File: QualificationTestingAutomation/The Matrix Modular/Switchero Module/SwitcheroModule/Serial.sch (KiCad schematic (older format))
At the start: 13 parts, among them IC1 MAX3109ETJ+, Q2 2N7002DW

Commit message: Cleaned up the libraries Cleaned up the tracks Adjusted footprints to the manufacturers minimum size.
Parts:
- C1: symbol TheMatrix-rescue:CAP-passive-SchematicAutomation-rescue -> SwitcheroModule-rescue:CAP-passive-SchematicAutomation-rescue-TheMatrix-rescue
- Q2: symbol TheMatrix-rescue:2N7002DW-dk_Transistors-FETs-MOSFETs-Arrays-SchematicAutomation-rescue -> SwitcheroModule-rescue:2N7002DW-dk_Transistors-FETs-MOSFETs-Arrays-SchematicAutomation-rescue-TheMatrix-rescue
- R10, R11, R12, R7, R8, R9: symbol TheMatrix-rescue:RESISTOR-passive-SchematicAutomation-rescue -> SwitcheroModule-rescue:RESISTOR-passive-SchematicAutomation-rescue-TheMatrix-rescue
- S1, S2, S3, S4: symbol TheMatrix-rescue:ATE1D-2M3-10-Z-dk_Toggle-Switches-SchematicAutomation-rescue -> SwitcheroModule-rescue:ATE1D-2M3-10-Z-dk_Toggle-Switches-SchematicAutomation-rescue-TheMatrix-rescue
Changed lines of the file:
@@
 ADD LEDS!!!!
 $Comp
-L TheMatrix-rescue:ATE1D-2M3-10-Z-dk_Toggle-Switches-SchematicAutomation-rescue S?
+L SwitcheroModule-rescue:ATE1D-2M3-10-Z-dk_Toggle-Switches-SchematicAutomation-rescue-TheMatrix-rescue S?
 U 1 1 5CB40D46
 P 3700 2600
@@
 	3200 2850 3450 2850
 $Comp
-L TheMatrix-rescue:ATE1D-2M3-10-Z-dk_Toggle-Switches-SchematicAutomation-rescue S?
+L SwitcheroModule-rescue:ATE1D-2M3-10-Z-dk_Toggle-Switches-SchematicAutomation-rescue-TheMatrix-rescue S?
 U 1 1 5CB40D93
 P 3650 3200
@@
 $EndComp
 $Comp
-L TheMatrix-rescue:ATE1D-2M3-10-Z-dk_Toggle-Switches-SchematicAutomation-rescue S?
+L SwitcheroModule-rescue:ATE1D-2M3-10-Z-dk_Toggle-Switches-SchematicAutomation-rescue-TheMatrix-rescue S?
 U 1 1 5CB40DA3
 P 4350 3700
@@
 $EndComp
 $Comp
-L TheMatrix-rescue:ATE1D-2M3-10-Z-dk_Toggle-Switches-SchematicAutomation-rescue S?
+L SwitcheroModule-rescue:ATE1D-2M3-10-Z-dk_Toggle-Switches-SchematicAutomation-rescue-TheMatrix-rescue S?
 U 1 1 5CB40DBC
 P 4300 2700
@@
 	4650 2600 4500 2600
 $Comp
-L TheMatrix-rescue:2N7002DW-dk_Transistors-FETs-MOSFETs-Arrays-SchematicAutomation-rescue Q?
+L SwitcheroModule-rescue:2N7002DW-dk_Transistors-FETs-MOSFETs-Arrays-SchematicAutomation-rescue-TheMatrix-rescue Q?
 U 1 1 5CA046D4
 P 2500 4500
@@
 AR Path="/5C90F514/5C94ECF2/5CA046D4" Ref="Q?"  Part="1"
 AR Path="/5C90F514/5CA046D4" Ref="Q2"  Part="1"
+AR Path="/5CA046D4" Ref="Q2"  Part="1"
 F 0 "Q2" H 2500 4987 60  0000 C CNN
 F 1 "2N7002DW" H 2500 4881 60  0000 C CNN
@@
 RS232INV
 $Comp
-L TheMatrix-rescue:RESISTOR-passive-SchematicAutomation-rescue R?
+L SwitcheroModule-rescue:RESISTOR-passive-SchematicAutomation-rescue-TheMatrix-rescue R?
 U 1 1 5CA046DE
 P 3100 4600
@@
 	3000 4600 2950 4600
 $Comp
-L TheMatrix-rescue:RESISTOR-passive-SchematicAutomation-rescue R?
+L SwitcheroModule-rescue:RESISTOR-passive-SchematicAutomation-rescue-TheMatrix-rescue R?
 U 1 1 5CA046E9
 P 2950 4700
@@
 $EndComp
 $Comp
-L TheMatrix-rescue:RESISTOR-passive-SchematicAutomation-rescue R?
+L SwitcheroModule-rescue:RESISTOR-passive-SchematicAutomation-rescue-TheMatrix-rescue R?
 U 1 1 5CA046FA
 P 2000 4900
@@
 	6800 2550 6800 2650
 $Comp
-L TheMatrix-rescue:CAP-passive-SchematicAutomation-rescue C?
+L SwitcheroModule-rescue:CAP-passive-SchematicAutomation-rescue-TheMatrix-rescue C?
 U 1 1 5CB0095F
 P 6400 2550
@@
 $EndComp
 $Comp
-L TheMatrix-rescue:RESISTOR-passive-SchematicAutomation-rescue R?
+L SwitcheroModule-rescue:RESISTOR-passive-SchematicAutomation-rescue-TheMatrix-rescue R?
 U 1 1 5CB06957
 P 6300 5150
@@
 SSINV
 $Comp
-L TheMatrix-rescue:RESISTOR-passive-SchematicAutomation-rescue R?
+L SwitcheroModule-rescue:RESISTOR-passive-SchematicAutomation-rescue-TheMatrix-rescue R?
 U 1 1 5CB11DAA
 P 3150 4300
@@
 SSINV
 $Comp
-L TheMatrix-rescue:RESISTOR-passive-SchematicAutomation-rescue R?
+L SwitcheroModule-rescue:RESISTOR-passive-SchematicAutomation-rescue-TheMatrix-rescue R?
 U 1 1 5CB232AB
 P 5650 3650

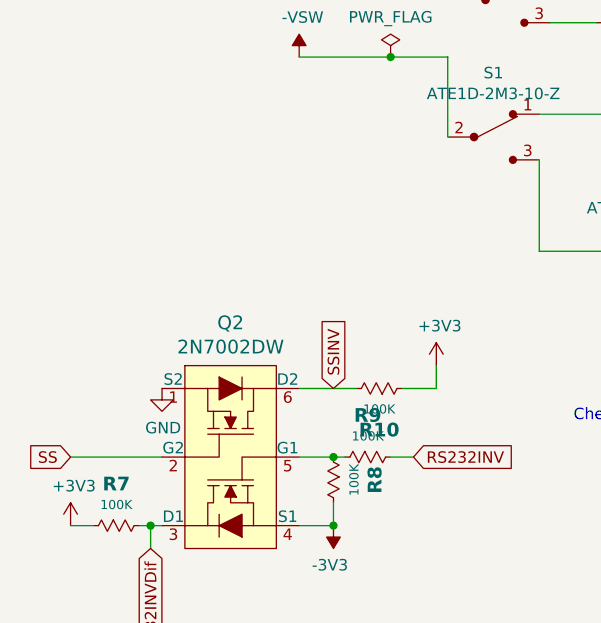
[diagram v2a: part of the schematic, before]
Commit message: Schematic Clean ups the layout needs to be changed
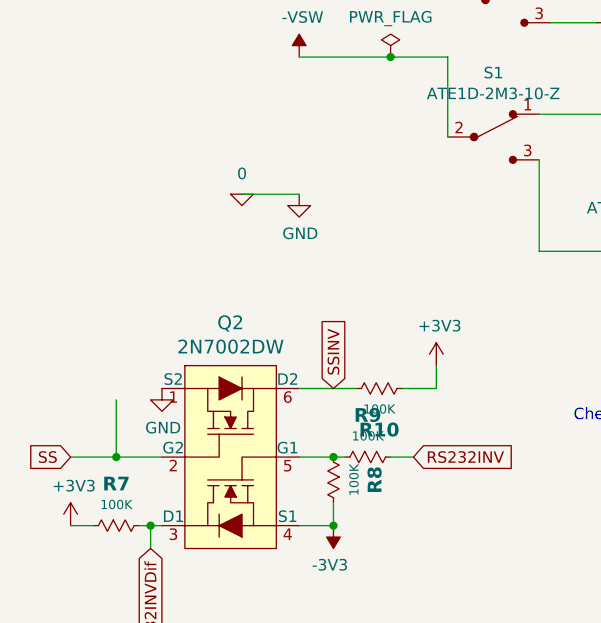
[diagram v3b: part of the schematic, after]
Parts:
- Q2: Spice_Lib_File (none) -> 2n7002dw.lib; Spice_Model (none) -> 2N7002DW; Spice_Netlist_Enabled (none) -> Y; Spice_Primitive (none) -> M
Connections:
- net GND renamed 0
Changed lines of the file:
@@
 F 11 "ON Semiconductor" H 2700 5600 60  0001 L CNN "Manufacturer"
 F 12 "Active" H 2700 5700 60  0001 L CNN "Status"
+F 13 "M" H 2500 4500 50  0001 C CNN "Spice_Primitive"
+F 14 "2N7002DW" H 2500 4500 50  0001 C CNN "Spice_Model"
+F 15 "Y" H 2500 4500 50  0001 C CNN "Spice_Netlist_Enabled"
+F 16 "2n7002dw.lib" H 2500 4500 50  0001 C CNN "Spice_Lib_File"
 	1    2500 4500
 	1    0    0    -1
@@
 SS
 Wire Wire Line
-	1800 4600 2200 4600
+	1800 4600 2000 4600
 Text GLabel 2950 4300 1    50   Input ~ 0
 SSINV
@@
 F 2 "" H 3400 4200 50  0001 C CNN
 F 3 "" H 3400 4200 50  0001 C CNN
+F 4 "V" H 3400 4200 50  0001 C CNN "Spice_Primitive"
+F 5 "dc 3.3" H 3400 4200 50  0001 C CNN "Spice_Model"
+F 6 "Y" H 3400 4200 50  0001 C CNN "Spice_Netlist_Enabled"
 	1    3400 4200
 	1    0    0    -1
@@
 	1    0    0    -1
 $EndComp
+$Comp
+L pspice:0 #GND0101
+U 1 1 5CB0FA23
+P 2550 3450
+F 0 "#GND0101" H 2550 3350 50  0001 C CNN
+F 1 "0" H 2550 3539 50  0000 C CNN
+F 2 "" H 2550 3450 50  0001 C CNN
+F 3 "~" H 2550 3450 50  0001 C CNN
+	1    2550 3450
+	1    0    0    -1
+$EndComp
+$Comp
+L power:GND #PWR?
+U 1 1 5CB10324
+P 2800 3450
+AR Path="/5C8DF48C/5CB10324" Ref="#PWR?"  Part="1"
+AR Path="/5C90F514/5CB10324" Ref="#PWR0232"  Part="1"
+F 0 "#PWR0232" H 2800 3200 50  0001 C CNN
+F 1 "GND" H 2805 3277 50  0000 C CNN
+F 2 "" H 2800 3450 50  0001 C CNN
+F 3 "" H 2800 3450 50  0001 C CNN
+	1    2800 3450
+	1    0    0    -1
+$EndComp
+Wire Wire Line
+	2800 3450 2550 3450
+Wire Wire Line
+	2000 4350 2000 4600
+Connection ~ 2000 4600
+Wire Wire Line
+	2000 4600 2200 4600
 $EndSCHEMATC

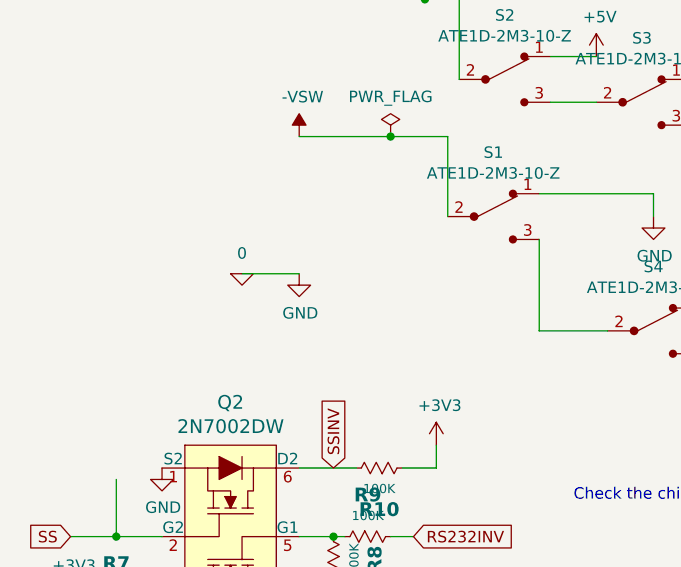
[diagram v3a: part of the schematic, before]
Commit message: IO clean up added the 1v25 reference to Matrix Changed Some of the labels to more legible names.
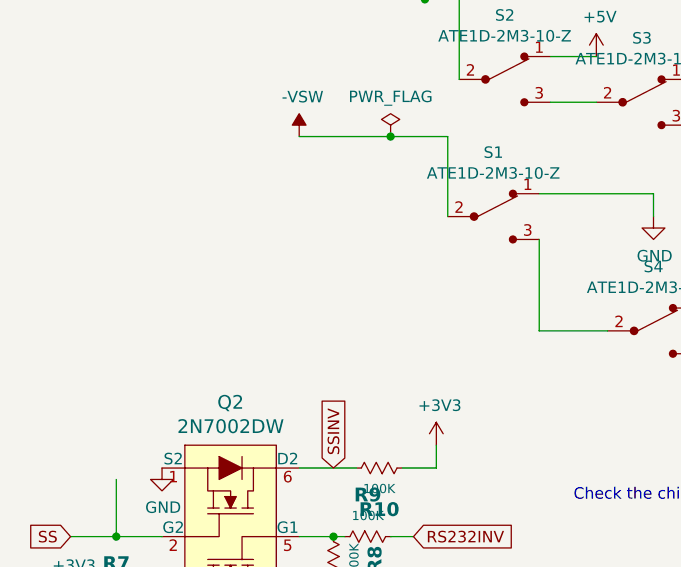
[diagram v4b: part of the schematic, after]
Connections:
- net 0 renamed GND
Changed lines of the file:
@@
-	1    0    0    -1
-$EndComp
-$Comp
-L pspice:0 #GND0101
-U 1 1 5CB0FA23
-P 2550 3450
-F 0 "#GND0101" H 2550 3350 50  0001 C CNN
-F 1 "0" H 2550 3539 50  0000 C CNN
-F 2 "" H 2550 3450 50  0001 C CNN
-F 3 "~" H 2550 3450 50  0001 C CNN
-	1    2550 3450
-	1    0    0    -1
-$EndComp
-$Comp
-L power:GND #PWR?
-U 1 1 5CB10324
-P 2800 3450
-AR Path="/5C8DF48C/5CB10324" Ref="#PWR?"  Part="1"
-AR Path="/5C90F514/5CB10324" Ref="#PWR0232"  Part="1"
-F 0 "#PWR0232" H 2800 3200 50  0001 C CNN
-F 1 "GND" H 2805 3277 50  0000 C CNN
-F 2 "" H 2800 3450 50  0001 C CNN
-F 3 "" H 2800 3450 50  0001 C CNN
-	1    2800 3450
 	1    0    0    -1
 $EndComp
 Wire Wire Line
-	2800 3450 2550 3450
-Wire Wire Line
 	2000 4350 2000 4600

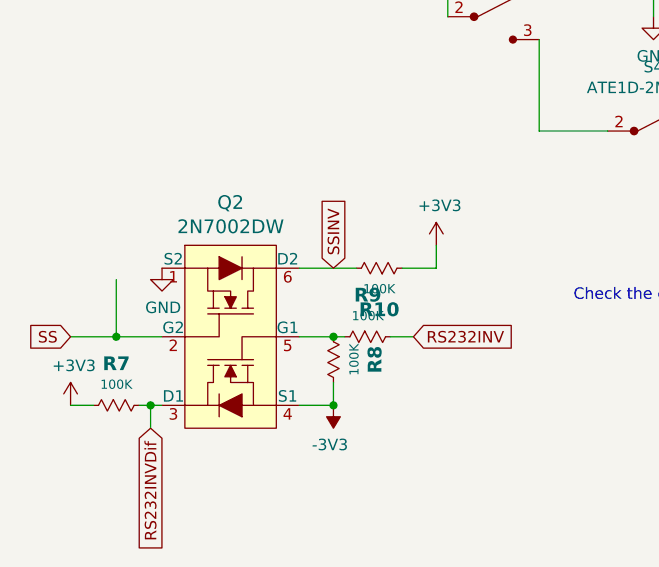
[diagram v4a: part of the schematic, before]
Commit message: Reefero Module PCB design
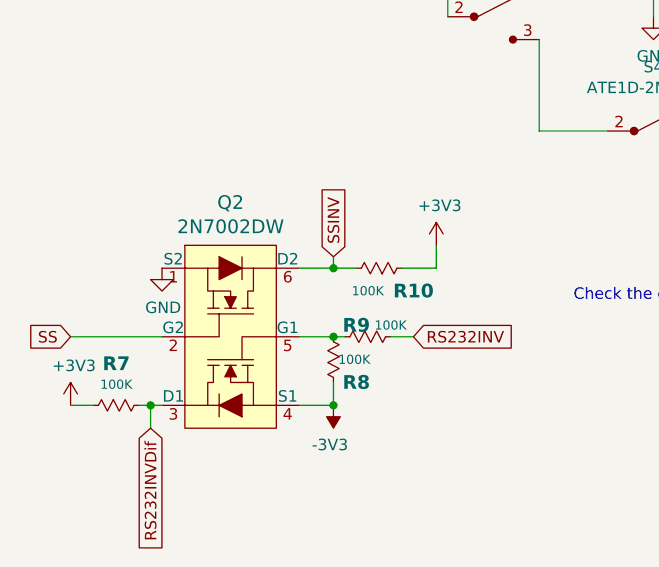
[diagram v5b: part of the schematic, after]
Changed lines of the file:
@@
 AR Path="/5C90F514/5C94ECF2/5CA046DE" Ref="R?"  Part="1"
 AR Path="/5C90F514/5CA046DE" Ref="R9"  Part="1"
-F 0 "R9" H 3100 4782 60  0000 C CNB
-F 1 "100K" H 3100 4691 40  0000 C CNN
+F 0 "R9" H 3050 4650 60  0000 C CNB
+F 1 "100K" H 3200 4650 40  0000 C CNN
 F 2 "Resistor_SMD:R_0402_1005Metric" H 3100 4460 40  0001 C CNN
 F 3 "" H 3100 4700 60  0000 C CNN
@@
 AR Path="/5C90F514/5C94ECF2/5CA046E9" Ref="R?"  Part="1"
 AR Path="/5C90F514/5CA046E9" Ref="R8"  Part="1"
-F 0 "R8" H 2950 4882 60  0000 C CNB
-F 1 "100K" H 2950 4791 40  0000 C CNN
+F 0 "R8" V 3050 4800 60  0000 C CNB
+F 1 "100K" V 2950 4791 40  0000 C CNN
 F 2 "Resistor_SMD:R_0402_1005Metric" H 2950 4560 40  0001 C CNN
 F 3 "" H 2950 4800 60  0000 C CNN
@@
 Text GLabel 1800 4600 0    50   Input ~ 0
 SS
-Wire Wire Line
-	1800 4600 2000 4600
-Text GLabel 2950 4300 1    50   Input ~ 0
+Text GLabel 2950 4250 1    50   Input ~ 0
 SSINV
 $Comp
@@
 AR Path="/5C90F514/5C94ECF2/5CB11DAA" Ref="R?"  Part="1"
 AR Path="/5C90F514/5CB11DAA" Ref="R10"  Part="1"
-F 0 "R10" H 3150 4482 60  0000 C CNB
-F 1 "100K" H 3150 4391 40  0000 C CNN
+F 0 "R10" H 3000 4400 60  0000 C CNB
+F 1 "100K" H 3200 4400 40  0000 C CNN
 F 2 "Resistor_SMD:R_0402_1005Metric" H 3150 4160 40  0001 C CNN
 F 3 "" H 3150 4400 60  0000 C CNN
@@
 	3400 4300 3400 4200
 Wire Wire Line
-	2800 4300 3050 4300
+	2800 4300 2950 4300
 Text GLabel 6100 4050 0    50   Input ~ 0
 SSINV
@@
 $EndComp
 Wire Wire Line
-	2000 4350 2000 4600
-Connection ~ 2000 4600
-Wire Wire Line
-	2000 4600 2200 4600
+	1800 4600 2200 4600
+Wire Wire Line
+	2950 4300 2950 4250
+Connection ~ 2950 4300
+Wire Wire Line
+	2950 4300 3050 4300
 $EndSCHEMATC
